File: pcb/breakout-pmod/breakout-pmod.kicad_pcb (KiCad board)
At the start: 4 copper layers, 88.9 x 100 mm, 13 parts, among them J1 FX18-120P-0.8SV20

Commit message: [pmod] fix order of BA pmod
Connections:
- J1 pad 64: /BA_02 -> /BA_05
- J1 pad 65: /BA_03 -> /BA_02
- J1 pad 66: /BA_04 -> /BA_06
- J1 pad 67: /BA_05 -> /BA_03
- J1 pad 68: /BA_06 -> /BA_07
- J1 pad 69: /BA_07 -> /BA_04
- PM12 pad 2: /BA_03 -> /BA_02
- PM12 pad 3: /BA_05 -> /BA_03
- PM12 pad 4: /BA_07 -> /BA_04
- PM12 pad 7: /BA_02 -> /BA_05
- PM12 pad 8: /BA_04 -> /BA_06
- PM12 pad 9: /BA_06 -> /BA_07
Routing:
- net /BA_07: track 76.9 -> 79.8 mm
- net /BA_02: track 79.0 -> 76.1 mm
- net /BA_05: track 76.5 -> 79.0 mm
- net /BA_04: track 79.4 -> 76.9 mm
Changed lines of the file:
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@@
 			(size 0.4572 2.2098)
 			(layers "F.Cu" "F.Paste" "F.Mask")
-			(net 48 "/BA_02")
+			(net 54 "/BA_05")
 			(pinfunction "64")
 			(pintype "passive")
@@
 			(size 0.4572 2.2098)
 			(layers "F.Cu" "F.Paste" "F.Mask")
-			(net 84 "/BA_03")
+			(net 48 "/BA_02")
 			(pinfunction "65")
 			(pintype "passive")
@@
 			(size 0.4572 2.2098)
 			(layers "F.Cu" "F.Paste" "F.Mask")
-			(net 52 "/BA_04")
+			(net 64 "/BA_06")
 			(pinfunction "66")
 			(pintype "passive")
@@
 			(size 0.4572 2.2098)
 			(layers "F.Cu" "F.Paste" "F.Mask")
-			(net 54 "/BA_05")
+			(net 84 "/BA_03")
 			(pinfunction "67")
 			(pintype "passive")
@@
 			(size 0.4572 2.2098)
 			(layers "F.Cu" "F.Paste" "F.Mask")
-			(net 64 "/BA_06")
+			(net 66 "/BA_07")
 			(pinfunction "68")
 			(pintype "passive")
@@
 			(size 0.4572 2.2098)
 			(layers "F.Cu" "F.Paste" "F.Mask")
-			(net 66 "/BA_07")
+			(net 52 "/BA_04")
 			(pinfunction "69")
 			(pintype "passive")
@@
 			(layers "*.Cu" "*.Mask")
 			(remove_unused_layers no)
-			(net 84 "/BA_03")
+			(net 48 "/BA_02")
 			(pinfunction "Pin_2")
 			(pintype "passive")
@@
 			(layers "*.Cu" "*.Mask")
 			(remove_unused_layers no)
-			(net 54 "/BA_05")
+			(net 84 "/BA_03")
 			(pinfunction "Pin_3")
 			(pintype "passive")
@@
 			(layers "*.Cu" "*.Mask")
 			(remove_unused_layers no)
-			(net 66 "/BA_07")
+			(net 52 "/BA_04")
 			(pinfunction "Pin_4")
 			(pintype "passive")
@@
 			(layers "*.Cu" "*.Mask")
 			(remove_unused_layers no)
-			(net 48 "/BA_02")
+			(net 54 "/BA_05")
 			(pinfunction "Pin_7")
 			(pintype "passive")
@@
 			(layers "*.Cu" "*.Mask")
 			(remove_unused_layers no)
-			(net 52 "/BA_04")
+			(net 64 "/BA_06")
 			(pinfunction "Pin_8")
 			(pintype "passive")
@@
 			(layers "*.Cu" "*.Mask")
 			(remove_unused_layers no)
-			(net 64 "/BA_06")
+			(net 66 "/BA_07")
 			(pinfunction "Pin_9")
 			(pintype "passive")
@@
 		)
 	)
-	(gr_text "05/09"
+	(gr_text "03/07"
 		(at 114.935 78.994 0)
 		(layer "F.SilkS")
@@
 		)
 	)
-	(gr_text "06/10"
+	(gr_text "04/08"
 		(at 114.935 81.534 0)
 		(layer "F.SilkS")
@@
 		)
 	)
-	(gr_text "02/08"
+	(gr_text "02/06"
 		(at 114.935 76.454 0)
 		(layer "F.SilkS")
@@
 		)
 	)
-	(gr_text "01/07"
+	(gr_text "01/05"
 		(at 114.935 73.914 0)
 		(layer "F.SilkS")
@@
 	)
 	(segment
-		(start 48.741996 70.130004)
-		(end 48.768 70.104)
+		(start 46.851001 70.930003)
+		(end 48.800003 70.930003)
 		(width 0.156464)
 		(layer "F.Cu")
@@
 	)
 	(segment
-		(start 46.851001 70.130004)
-		(end 48.741996 70.130004)
+		(start 48.800003 70.930003)
+		(end 48.81 70.94)
 		(width 0.156464)
 		(layer "F.Cu")
@@
 	)
 	(via
-		(at 48.79 70.130004)
+		(at 48.79 70.930003)
 		(size 0.6096)
 		(drill 0.3048)
@@
 	)
 	(segment
-		(start 112.87 74.8)
-		(end 122.085 74.8)
-		(width 0.156464)
-		(layer "B.Cu")
-		(net 48)
-	)
-	(segment
-		(start 48.79 70.130004)
-		(end 108.200004 70.130004)
+		(start 48.79 70.930003)
+		(end 107.640003 70.930003)
 		(width 0.156464)
 		(layer "B.Cu")
@@
 	)
 	(segment
-		(start 108.200004 70.130004)
-		(end 112.87 74.8)
+		(start 112.74 76.03)
+		(end 120.855 76.03)
 		(width 0.156464)
 		(layer "B.Cu")
@@
 	)
 	(segment
-		(start 122.085 74.8)
-		(end 123.395 73.49)
+		(start 107.640003 70.930003)
+		(end 112.74 76.03)
 		(width 0.156464)
 		(layer "B.Cu")
@@
 	)
 	(segment
-		(start 48.789996 71.730004)
-		(end 48.81 71.71)
-		(width 0.156464)
-		(layer "F.Cu")
-		(net 52)
-	)
-	(segment
-		(start 46.851001 71.730004)
-		(end 48.789996 71.730004)
+		(start 48.83 74.130004)
+		(end 46.860997 74.130004)
 		(width 0.156464)
 		(layer "F.Cu")
@@
 	)
 	(via
-		(at 48.79 71.730004)
+		(at 48.79 74.130004)
 		(size 0.6096)
 		(drill 0.3048)
@@
 	)
 	(segment
-		(start 48.79 71.730004)
-		(end 107.020004 71.730004)
-		(width 0.156464)
-		(layer "B.Cu")
-		(net 52)
-	)
-	(segment
-		(start 112.61 77.32)
-		(end 122.105 77.32)
+		(start 105.372004 74.130004)
+		(end 112.352 81.11)
 		(width 0.156464)
 		(layer "B.Cu")
@@
 	)
 	(segment
-		(start 107.020004 71.730004)
-		(end 112.61 77.32)
+		(start 48.79 74.130004)
+		(end 105.372004 74.130004)
 		(width 0.156464)
 		(layer "B.Cu")
@@
 	)
 	(segment
-		(start 122.105 77.32)
-		(end 123.395 76.03)
+		(start 112.352 81.11)
+		(end 120.855 81.11)
 		(width 0.156464)
 		(layer "B.Cu")
@@
 	)
 	(segment
-		(start 48.8 72.530002)
-		(end 46.860999 72.530002)
+		(start 48.741996 70.130004)
+		(end 48.768 70.104)
+		(width 0.156464)
+		(layer "F.Cu")
+		(net 54)
+	)
+	(segment
+		(start 46.851001 70.130004)
+		(end 48.741996 70.130004)
 		(width 0.156464)
 		(layer "F.Cu")
@@
 	)
 	(via
-		(at 48.79 72.530002)
+		(at 48.79 70.130004)
 		(size 0.6096)
 		(drill 0.3048)
@@
 	)
 	(segment
-		(start 112.39 78.57)
-		(end 120.855 78.57)
+		(start 112.87 74.8)
+		(end 122.085 74.8)
 		(width 0.156464)
 		(layer "B.Cu")
@@
 	)
 	(segment
-		(start 48.79 72.530002)
-		(end 106.350002 72.530002)
+		(start 48.79 70.130004)
+		(end 108.200004 70.130004)
 		(width 0.156464)
 		(layer "B.Cu")
@@
 	)
 	(segment
-		(start 106.350002 72.530002)
-		(end 112.39 78.57)
+		(start 108.200004 70.130004)
+		(end 112.87 74.8)
+		(width 0.156464)
+		(layer "B.Cu")
+		(net 54)
+	)
+	(segment
+		(start 122.085 74.8)
+		(end 123.395 73.49)
 		(width 0.156464)
 		(layer "B.Cu")
@@
 	)
 	(segment
-		(start 46.851001 73.330003)
-		(end 48.799997 73.330003)
+		(start 48.789996 71.730004)
+		(end 48.81 71.71)
 		(width 0.156464)
 		(layer "F.Cu")
@@
 	)
 	(segment
-		(start 48.799997 73.330003)
-		(end 48.82 73.31)
+		(start 46.851001 71.730004)
+		(end 48.789996 71.730004)
 		(width 0.156464)
 		(layer "F.Cu")
@@
 	)
 	(via
-		(at 48.79 73.330003)
+		(at 48.79 71.730004)
 		(size 0.6096)
 		(drill 0.3048)
@@
 	)
 	(segment
-		(start 48.790003 73.33)
-		(end 105.842 73.33)
-		(width 0.156464)
-		(layer "B.Cu")
-		(net 64)
-	)
-	(segment
-		(start 48.79 73.330003)
-		(end 48.790003 73.33)
+		(start 48.79 71.730004)
+		(end 107.020004 71.730004)
 		(width 0.156464)
 		(layer "B.Cu")
@@
 	)
 	(segment
-		(start 105.842 73.33)
-		(end 112.372 79.86)
+		(start 112.61 77.32)
+		(end 122.105 77.32)
 		(width 0.156464)
 		(layer "B.Cu")
@@
 	)
 	(segment
-		(start 112.372 79.86)
-		(end 122.105 79.86)
+		(start 107.020004 71.730004)
+		(end 112.61 77.32)
 		(width 0.156464)
 		(layer "B.Cu")
@@
 	)
 	(segment
-		(start 122.105 79.86)
-		(end 123.395 78.57)
+		(start 122.105 77.32)
+		(end 123.395 76.03)
 		(width 0.156464)
 		(layer "B.Cu")
@@
 	)
 	(segment
-		(start 48.83 74.130004)
-		(end 46.860997 74.130004)
+		(start 46.851001 73.330003)
+		(end 48.799997 73.330003)
+		(width 0.156464)
+		(layer "F.Cu")
+		(net 66)
+	)
+	(segment
+		(start 48.799997 73.330003)
+		(end 48.82 73.31)
 		(width 0.156464)
 		(layer "F.Cu")
@@
 	)
 	(via
-		(at 48.79 74.130004)
+		(at 48.79 73.330003)
 		(size 0.6096)
 		(drill 0.3048)
@@
 	)
 	(segment
-		(start 105.372004 74.130004)
-		(end 112.352 81.11)
+		(start 48.790003 73.33)
+		(end 105.842 73.33)
 		(width 0.156464)
 		(layer "B.Cu")
@@
 	)
 	(segment
-		(start 48.79 74.130004)
-		(end 105.372004 74.130004)
+		(start 48.79 73.330003)
+		(end 48.790003 73.33)
 		(width 0.156464)
 		(layer "B.Cu")
@@
 	)
 	(segment
-		(start 112.352 81.11)
-		(end 120.855 81.11)
+		(start 105.842 73.33)
+		(end 112.372 79.86)
+		(width 0.156464)
+		(layer "B.Cu")
+		(net 66)
+	)
+	(segment
+		(start 112.372 79.86)
+		(end 122.105 79.86)
+		(width 0.156464)
+		(layer "B.Cu")
+		(net 66)
+	)
+	(segment
+		(start 122.105 79.86)
+		(end 123.395 78.57)
 		(width 0.156464)
 		(layer "B.Cu")
@@
 	)
 	(segment
-		(start 46.851001 70.930003)
-		(end 48.800003 70.930003)
-		(width 0.156464)
-		(layer "F.Cu")
-		(net 84)
-	)
-	(segment
-		(start 48.800003 70.930003)
-		(end 48.81 70.94)
+		(start 48.8 72.530002)
+		(end 46.860999 72.530002)
 		(width 0.156464)
 		(layer "F.Cu")
@@
 	)
 	(via
-		(at 48.79 70.930003)
+		(at 48.79 72.530002)
 		(size 0.6096)
 		(drill 0.3048)
@@
 	)
 	(segment
-		(start 48.79 70.930003)
-		(end 107.640003 70.930003)
+		(start 112.39 78.57)
+		(end 120.855 78.57)
 		(width 0.156464)
 		(layer "B.Cu")
@@
 	)
 	(segment
-		(start 112.74 76.03)
-		(end 120.855 76.03)
+		(start 48.79 72.530002)
+		(end 106.350002 72.530002)
 		(width 0.156464)
 		(layer "B.Cu")
@@
 	)
 	(segment
-		(start 107.640003 70.930003)
-		(end 112.74 76.03)
+		(start 106.350002 72.530002)
+		(end 112.39 78.57)
 		(width 0.156464)
 		(layer "B.Cu")

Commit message: [pmod] fix order of DC pmod
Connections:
- J1 pad 74: /DC_02 -> /DC_05
- J1 pad 75: /DC_03 -> /DC_02
- J1 pad 76: /DC_04 -> /DC_06
- J1 pad 77: /DC_05 -> /DC_03
- J1 pad 78: /DC_06 -> /DC_07
- J1 pad 79: /DC_07 -> /DC_04
- PM11 pad 2: /DC_03 -> /DC_02
- PM11 pad 3: /DC_05 -> /DC_03
- PM11 pad 4: /DC_07 -> /DC_04
- PM11 pad 7: /DC_02 -> /DC_05
- PM11 pad 8: /DC_04 -> /DC_06
- PM11 pad 9: /DC_06 -> /DC_07
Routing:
- net /DC_02: track 85.1 -> 82.3 mm
- net /DC_07: track 83.2 -> 85.8 mm
- net /DC_05: track 82.8 -> 85.1 mm
- net /DC_04: track 85.4 -> 83.2 mm

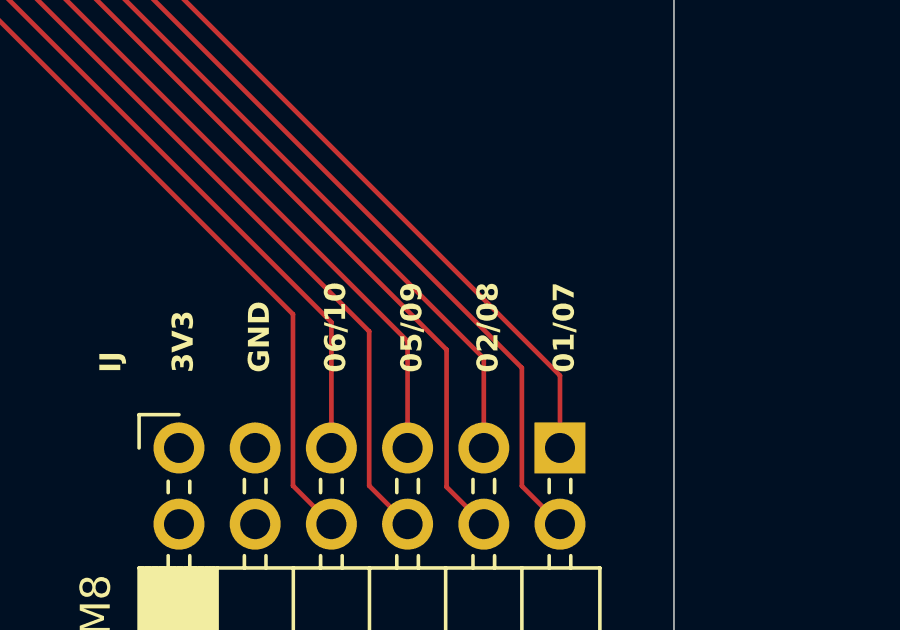
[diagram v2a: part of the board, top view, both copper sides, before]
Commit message: [pmod] fix order of IJ pmod
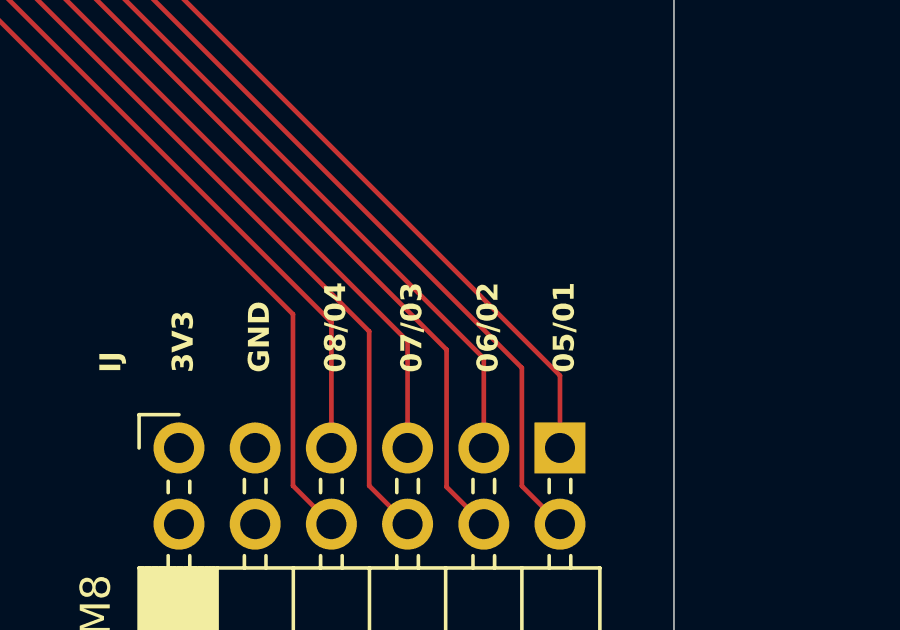
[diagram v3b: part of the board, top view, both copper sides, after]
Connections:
- J1 pad 42: /IJ_02 -> /IJ_05
- J1 pad 43: /IJ_03 -> /IJ_02
- J1 pad 44: /IJ_04 -> /IJ_06
- J1 pad 45: /IJ_05 -> /IJ_03
- J1 pad 46: /IJ_06 -> /IJ_07
- J1 pad 47: /IJ_07 -> /IJ_04
- PM8 pad 2: /IJ_03 -> /IJ_02
- PM8 pad 3: /IJ_05 -> /IJ_03
- PM8 pad 4: /IJ_07 -> /IJ_04
- PM8 pad 7: /IJ_02 -> /IJ_05
- PM8 pad 8: /IJ_04 -> /IJ_06
- PM8 pad 9: /IJ_06 -> /IJ_07
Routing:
- net /IJ_05: track 84.2 -> 91.5 mm
- net /IJ_04: track 88.7 -> 81.3 mm
- net /IJ_02: track 91.5 -> 86.1 mm
- net /IJ_07: track 81.3 -> 85.8 mm
- net /IJ_06: track 85.8 -> 88.7 mm
- net /IJ_03: track 86.1 -> 84.2 mm
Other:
- board text added: "05/01"
- board text added: "06/02"
- board text added: "07/03"
- board text added: "08/04"
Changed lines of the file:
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@@
 			(size 0.4572 2.2098)
 			(layers "F.Cu" "F.Paste" "F.Mask")
-			(net 65 "/IJ_02")
+			(net 57 "/IJ_05")
 			(pinfunction "42")
 			(pintype "passive")
@@
 			(size 0.4572 2.2098)
 			(layers "F.Cu" "F.Paste" "F.Mask")
-			(net 98 "/IJ_03")
+			(net 65 "/IJ_02")
 			(pinfunction "43")
 			(pintype "passive")
@@
 			(size 0.4572 2.2098)
 			(layers "F.Cu" "F.Paste" "F.Mask")
-			(net 1 "/IJ_04")
+			(net 44 "/IJ_06")
 			(pinfunction "44")
 			(pintype "passive")
@@
 			(size 0.4572 2.2098)
 			(layers "F.Cu" "F.Paste" "F.Mask")
-			(net 57 "/IJ_05")
+			(net 98 "/IJ_03")
 			(pinfunction "45")
 			(pintype "passive")
@@
 			(size 0.4572 2.2098)
 			(layers "F.Cu" "F.Paste" "F.Mask")
-			(net 44 "/IJ_06")
+			(net 8 "/IJ_07")
 			(pinfunction "46")
 			(pintype "passive")
@@
 			(size 0.4572 2.2098)
 			(layers "F.Cu" "F.Paste" "F.Mask")
-			(net 8 "/IJ_07")
+			(net 1 "/IJ_04")
 			(pinfunction "47")
 			(pintype "passive")
@@
 			(layers "*.Cu" "*.Mask")
 			(remove_unused_layers no)
-			(net 98 "/IJ_03")
+			(net 65 "/IJ_02")
 			(pinfunction "Pin_2")
 			(pintype "passive")
@@
 			(layers "*.Cu" "*.Mask")
 			(remove_unused_layers no)
-			(net 57 "/IJ_05")
+			(net 98 "/IJ_03")
 			(pinfunction "Pin_3")
 			(pintype "passive")
@@
 			(layers "*.Cu" "*.Mask")
 			(remove_unused_layers no)
-			(net 8 "/IJ_07")
+			(net 1 "/IJ_04")
 			(pinfunction "Pin_4")
 			(pintype "passive")
@@
 			(layers "*.Cu" "*.Mask")
 			(remove_unused_layers no)
-			(net 65 "/IJ_02")
+			(net 57 "/IJ_05")
 			(pinfunction "Pin_7")
 			(pintype "passive")
@@
 			(layers "*.Cu" "*.Mask")
 			(remove_unused_layers no)
-			(net 1 "/IJ_04")
+			(net 44 "/IJ_06")
 			(pinfunction "Pin_8")
 			(pintype "passive")
@@
 			(layers "*.Cu" "*.Mask")
 			(remove_unused_layers no)
-			(net 44 "/IJ_06")
+			(net 8 "/IJ_07")
 			(pinfunction "Pin_9")
 			(pintype "passive")
@@
 		)
 	)
-	(gr_text "01/07"
+	(gr_text "05/01"
 		(at 130.683 124.968 90)
 		(layer "F.SilkS")
@@
 		)
 	)
-	(gr_text "06/10"
+	(gr_text "08/04"
 		(at 123.063 124.968 90)
 		(layer "F.SilkS")
@@
 		)
 	)
-	(gr_text "05/09"
+	(gr_text "07/03"
 		(at 125.603 124.968 90)
 		(layer "F.SilkS")
@@
 		)
 	)
-	(gr_text "02/08"
+	(gr_text "06/02"
 		(at 128.143 124.968 90)
 		(layer "F.SilkS")
@@
 	)
 	(segment
-		(start 53.150999 102.129999)
-		(end 104.288999 102.129999)
-		(width 0.156464)
-		(layer "F.Cu")
-		(net 1)
-	)
-	(segment
-		(start 126.36 124.201)
-		(end 126.36 128.775)
+		(start 53.150999 104.529996)
+		(end 103.767996 104.529996)
 		(width 0.156464)
 		(layer "F.Cu")
@@
 	)
 	(segment
-		(start 104.288999 102.129999)
-		(end 126.36 124.201)
+		(start 122.52 123.282)
+		(end 122.52 127.475)
 		(width 0.156464)
 		(layer "F.Cu")
@@
 	)
 	(segment
-		(start 126.36 128.775)
-		(end 127.6 130.015)
+		(start 103.767996 104.529996)
+		(end 122.52 123.282)
 		(width 0.156464)
 		(layer "F.Cu")
@@
 	)
 	(segment
-		(start 53.150999 104.529996)
-		(end 103.767996 104.529996)
+		(start 123.78 128.735)
+		(end 125.06 130.015)
 		(width 0.156464)
 		(layer "F.Cu")
@@
 	)
 	(segment
-		(start 122.52 123.282)
-		(end 122.52 127.475)
+		(start 103.920498 103.729998)
+		(end 123.78 123.5895)
 		(width 0.156464)
 		(layer "F.Cu")
@@
 	)
 	(segment
-		(start 103.767996 104.529996)
-		(end 122.52 123.282)
+		(start 53.150999 103.729998)
+		(end 103.920498 103.729998)
+		(width 0.156464)
+		(layer "F.Cu")
+		(net 8)
+	)
+	(segment
+		(start 123.78 123.5895)
+		(end 123.78 128.735)
 		(width 0.156464)
 		(layer "F.Cu")
@@
 	)
 	(segment
-		(start 123.78 128.735)
-		(end 125.06 130.015)
+		(start 53.150999 102.129999)
+		(end 104.288999 102.129999)
 		(width 0.156464)
 		(layer "F.Cu")
@@
 	)
 	(segment
-		(start 103.920498 103.729998)
-		(end 123.78 123.5895)
+		(start 126.36 124.201)
+		(end 126.36 128.775)
 		(width 0.156464)
 		(layer "F.Cu")
@@
 	)
 	(segment
-		(start 53.150999 103.729998)
-		(end 103.920498 103.729998)
+		(start 104.288999 102.129999)
+		(end 126.36 124.201)
 		(width 0.156464)
 		(layer "F.Cu")
@@
 	)
 	(segment
-		(start 123.78 123.5895)
-		(end 123.78 128.735)
+		(start 126.36 128.775)
+		(end 127.6 130.015)
 		(width 0.156464)
 		(layer "F.Cu")
@@
 	)
 	(segment
-		(start 125.06 123.917)
-		(end 125.06 127.475)
+		(start 104.593997 100.529997)
+		(end 128.87 124.806)
 		(width 0.156464)
 		(layer "F.Cu")
@@
 	)
 	(segment
-		(start 53.150999 102.929997)
-		(end 104.072997 102.929997)
+		(start 128.87 128.745)
+		(end 130.14 130.015)
 		(width 0.156464)
 		(layer "F.Cu")
@@
 	)
 	(segment
-		(start 104.072997 102.929997)
-		(end 125.06 123.917)
+		(start 53.150999 100.529997)
+		(end 104.593997 100.529997)
+		(width 0.156464)
+		(layer "F.Cu")
+		(net 57)
+	)
+	(segment
+		(start 128.87 124.806)
+		(end 128.87 128.745)
 		(width 0.156464)
 		(layer "F.Cu")
@@
 	)
 	(segment
-		(start 104.593997 100.529997)
-		(end 128.87 124.806)
-		(width 0.156464)
-		(layer "F.Cu")
-		(net 65)
-	)
-	(segment
-		(start 128.87 128.745)
-		(end 130.14 130.015)
+		(start 127.6 124.4885)
+		(end 127.6 127.475)
 		(width 0.156464)
 		(layer "F.Cu")
@@
 	)
 	(segment
-		(start 53.150999 100.529997)
-		(end 104.593997 100.529997)
+		(start 54.043301 101.346)
+		(end 104.4575 101.346)
 		(width 0.156464)
 		(layer "F.Cu")
@@
 	)
 	(segment
-		(start 128.87 124.806)
-		(end 128.87 128.745)
+		(start 104.4575 101.346)
+		(end 127.6 124.4885)
 		(width 0.156464)
 		(layer "F.Cu")
@@
 	)
 	(segment
-		(start 127.6 124.4885)
-		(end 127.6 127.475)
+		(start 125.06 123.917)
+		(end 125.06 127.475)
 		(width 0.156464)
 		(layer "F.Cu")
@@
 	)
 	(segment
-		(start 54.043301 101.346)
-		(end 104.4575 101.346)
+		(start 53.150999 102.929997)
+		(end 104.072997 102.929997)
 		(width 0.156464)
 		(layer "F.Cu")
@@
 	)
 	(segment
-		(start 104.4575 101.346)
-		(end 127.6 124.4885)
+		(start 104.072997 102.929997)
+		(end 125.06 123.917)
 		(width 0.156464)
 		(layer "F.Cu")
